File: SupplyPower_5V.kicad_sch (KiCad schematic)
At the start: 5 parts, among them U1 K7805M-1000R3

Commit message: VER2.2: все изменения в списке изменений
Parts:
- D51: value +5V -> ~; Description P/N (none) -> Yellow LED; Product Name (none) -> FYLS-0805UYC; Purpose (none) -> +5V
- U1: value K7805M-1000R3 -> ~; Description P/N (none) -> DCDC converter; Product Name (none) -> K7805M-1000R3
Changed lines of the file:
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@@
+			)
+		)
+		(property "Description P/N" ""
+			(at 155.575 100.965 0)
+			(effects
+				(font
+					(size 1.27 1.27)
+				)
+			)
+		)
+		(property "Product Name" ""
+			(at 155.575 100.965 0)
+			(effects
+				(font
+					(size 1.27 1.27)
+				)
+			)
+		)
+		(property "Purpose" ""
+			(at 155.575 100.965 0)
+			(effects
+				(font
+					(size 1.27 1.27)
+				)
+			)
+		)
+		(property "Replacement" ""
+			(at 155.575 100.965 0)
+			(effects
+				(font
+					(size 1.27 1.27)
+				)
 			)
 		)
@@
 			)
 		)
+		(property "Description P/N" ""
+			(at 121.285 100.965 0)
+			(effects
+				(font
+					(size 1.27 1.27)
+				)
+			)
+		)
+		(property "Product Name" ""
+			(at 121.285 100.965 0)
+			(effects
+				(font
+					(size 1.27 1.27)
+				)
+			)
+		)
+		(property "Purpose" ""
+			(at 121.285 100.965 0)
+			(effects
+				(font
+					(size 1.27 1.27)
+				)
+			)
+		)
+		(property "Replacement" ""
+			(at 121.285 100.965 0)
+			(effects
+				(font
+					(size 1.27 1.27)
+				)
+			)
+		)
 		(pin "1"
 		)
@@
 			)
 		)
-		(property "Value" "+5V"
+		(property "Value" "~"
 			(at 166.878 103.378 90)
 			(effects
@@
 			)
 		)
+		(property "Description P/N" "Yellow LED"
+			(at 165.1 102.235 0)
+			(effects
+				(font
+					(size 1.27 1.27)
+				)
+				(hide yes)
+			)
+		)
+		(property "Product Name" "FYLS-0805UYC"
+			(at 165.1 102.235 0)
+			(effects
+				(font
+					(size 1.27 1.27)
+				)
+				(hide yes)
+			)
+		)
+		(property "Purpose" "+5V"
+			(at 165.1 102.235 0)
+			(effects
+				(font
+					(size 1.27 1.27)
+				)
+				(hide yes)
+			)
+		)
+		(property "Replacement" ""
+			(at 165.1 102.235 0)
+			(effects
+				(font
+					(size 1.27 1.27)
+				)
+				(hide yes)
+			)
+		)
 		(pin "1"
 		)
@@
 			)
 		)
+		(property "Description P/N" ""
+			(at 165.1 97.155 0)
+			(effects
+				(font
+					(size 1.27 1.27)
+				)
+			)
+		)
+		(property "Product Name" ""
+			(at 165.1 97.155 0)
+			(effects
+				(font
+					(size 1.27 1.27)
+				)
+			)
+		)
+		(property "Purpose" ""
+			(at 165.1 97.155 0)
+			(effects
+				(font
+					(size 1.27 1.27)
+				)
+			)
+		)
+		(property "Replacement" ""
+			(at 165.1 97.155 0)
+			(effects
+				(font
+					(size 1.27 1.27)
+				)
+			)
+		)
 		(pin "1"
 		)
@@
 		(on_board yes)
 		(dnp no)
-		(fields_autoplaced yes)
 		(property "Reference" "U1"
-			(at 142.24 84.455 90)
-			(effects
-				(font
-					(size 1 1)
-				)
-				(justify right)
-			)
-		)
-		(property "Value" "K7805M-1000R3"
+			(at 135.89 79.248 90)
+			(effects
+				(font
+					(size 1.27 1.27)
+				)
+			)
+		)
+		(property "Value" "~"
 			(at 142.24 86.995 90)
 			(effects
@@
 			(at 135.89 90.805 0)
 			(effects
+				(font
+					(size 1.27 1.27)
+				)
+				(hide yes)
+			)
+		)
+		(property "Description P/N" "DCDC converter"
+			(at 135.89 90.805 0)
+			(effects
+				(font
+					(size 1.27 1.27)
+				)
+				(hide yes)
+			)
+		)
+		(property "Product Name" "K7805M-1000R3"
+			(at 135.89 79.502 90)
+			(effects
+				(font
+					(size 1.27 1.27)
+				)
+				(hide yes)
+			)
+		)
+		(property "Purpose" ""
+			(at 135.89 90.805 0)
+			(effects
+				(font
+					(size 1.27 1.27)
+				)
+			)
+		)
+		(property "Replacement" ""
+			(at 135.89 90.805 0)
+			(effects

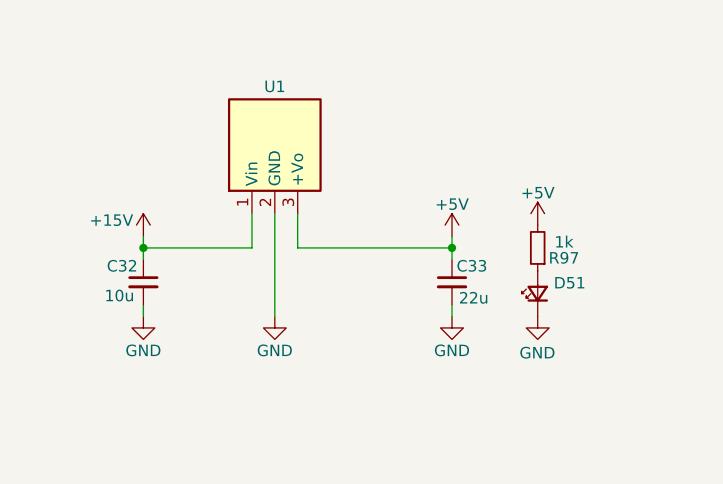
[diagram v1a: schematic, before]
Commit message: VER2.2: добавил фильтры на вход ШИМа и обновил все доки
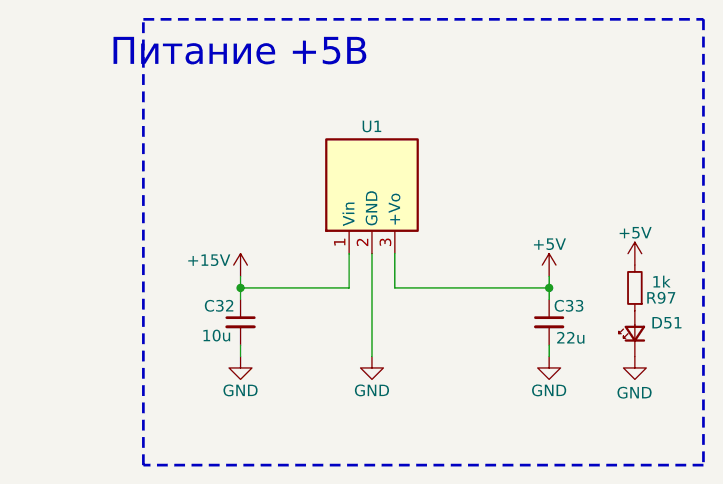
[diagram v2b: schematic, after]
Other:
- note added: "Питание +5В"
- company: (none) -> ООО "ЭТТ"
- moved on the sheet: C32, C33, D51, R97, U1

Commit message: VER2.2.1: создал папку для производственных доков
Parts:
- C32: Description P/N (none) -> Capacitor SMD 50+V
- C33: Description P/N (none) -> Capacitor SMD 25+V
- R97: Description P/N (none) -> Resistor SMD
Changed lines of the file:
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@@
 			)
 		)
-		(property "Description P/N" ""
+		(property "Description P/N" "Capacitor SMD 25+V"
 			(at 166.37 105.41 0)
 			(effects
@@
 			)
 		)
-		(property "Description P/N" ""
+		(property "Description P/N" "Capacitor SMD 50+V"
 			(at 132.08 105.41 0)
 			(effects
@@
 			)
 		)
-		(property "Description P/N" ""
+		(property "Description P/N" "Resistor SMD"
 			(at 175.895 101.6 0)
 			(effects
